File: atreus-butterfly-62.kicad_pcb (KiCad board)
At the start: 2 copper layers, 135.2 x 118.8 mm, 85 parts, among them J1 USB_OTG, J2 Conn_01x04, SW1 SW_Push, SW10 SW_Push, SW11 SW_Push, SW12 SW_Push, SW13 SW_Push, SW14 SW_Push, SW15 SW_Push, SW16 SW_Push, SW17 SW_Push, SW18 SW_Push, SW19 SW_Push, SW2 SW_Push, SW20 SW_Push, SW21 SW_Push, SW22 SW_Push, SW23 SW_Push, SW24 SW_Push, SW25 SW_Push, SW26 SW_Push, SW27 SW_Push, SW28 SW_Push, SW29 SW_Push, SW3 SW_Push, SW30 SW_Push, SW31 SW_Push, SW32 SW_Push, SW4 SW_Push, SW5 SW_Push, SW6 SW_Push, SW7 SW_Push, SW8 SW_Push, SW9 SW_Push, U1 ATMEGA32U4-MU, Y1 Crystal

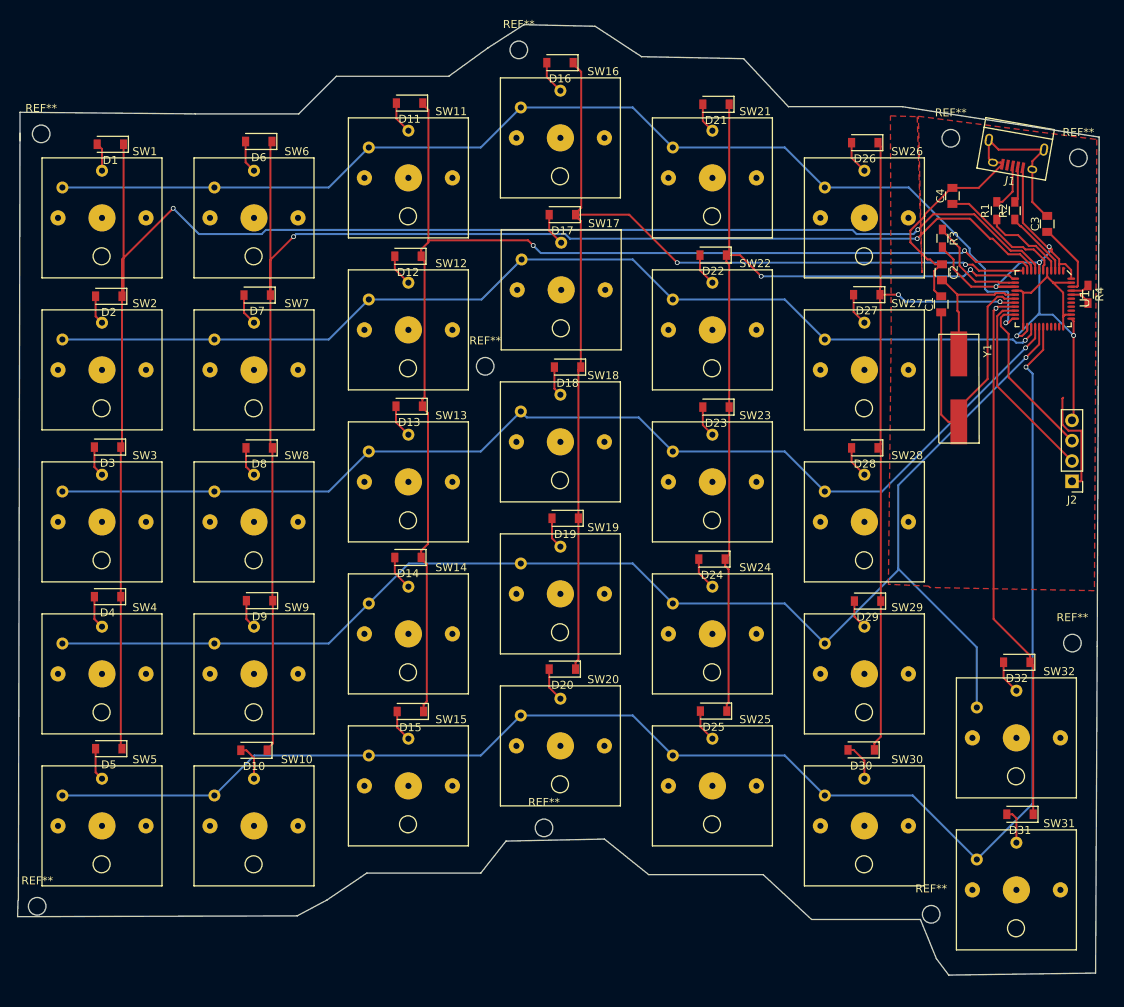
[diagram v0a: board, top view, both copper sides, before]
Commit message: delete middle keys and most traces
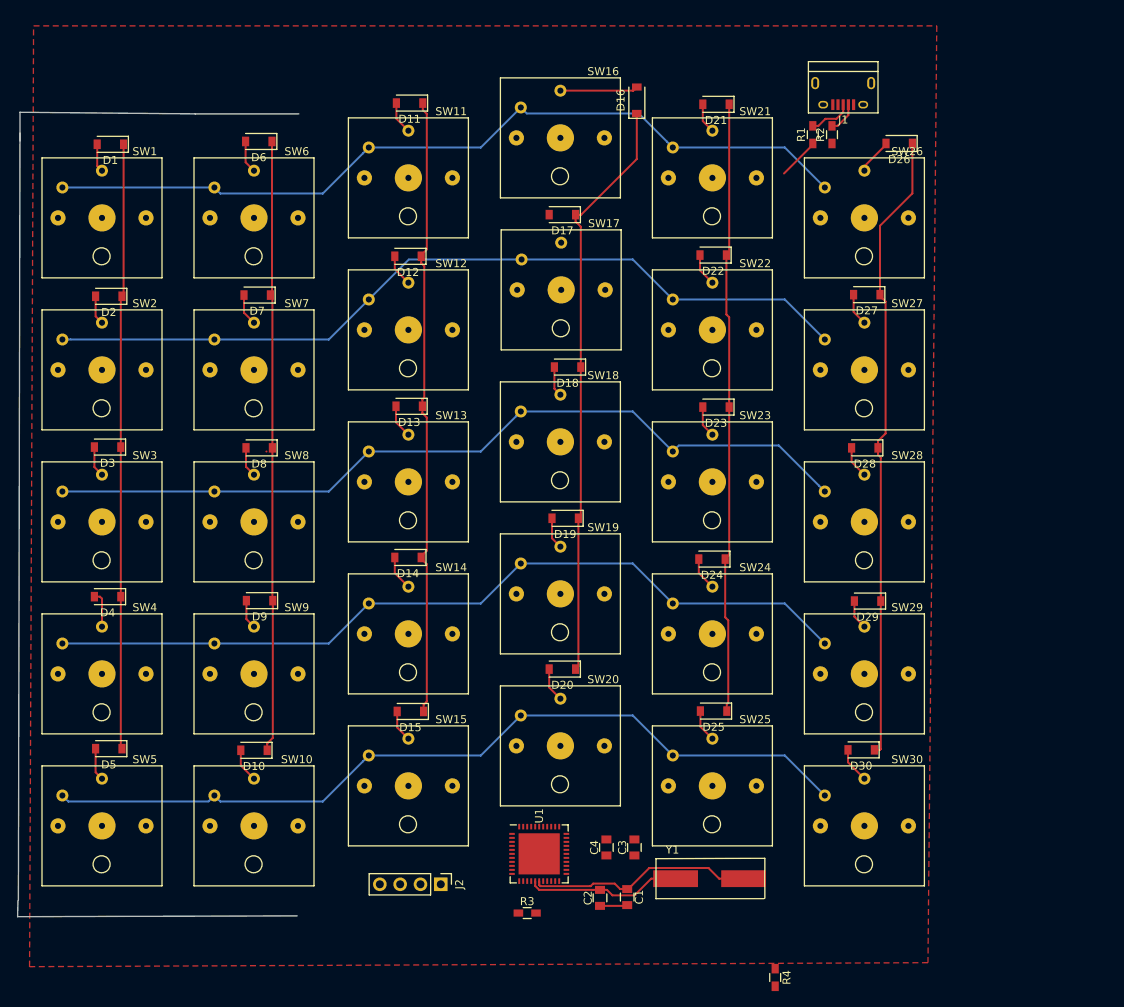
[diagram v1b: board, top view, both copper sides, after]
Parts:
- removed D31, D32: D, Diodes_SMD:D_SOD-123
- removed REF** (x9): MountingHole_2.2mm_M2, Mounting_Holes:MountingHole_2.2mm_M2
- removed SW31, SW32: SW_Push, ourglass_v7:Kailh_low_profile
- U1: footprint ourglass_v7:QFN_44 -> Housings_DFN_QFN:QFN-44-1EP_7x7mm_Pitch0.5mm
- moved R3 99.0 mm to (101.9, 152.0), turned to 0 degrees
- moved R4 93.9 mm to (132.9, 160.1)
- moved U1 93.7 mm to (103.4, 144.6), turned to 0 degrees
- moved J2 93.6 mm to (91.1, 148.4), turned to 270 degrees
- moved C3 93.5 mm to (115.3, 143.8)
- moved C4 92.2 mm to (111.8, 143.8)
- moved C2 89.1 mm to (111.0, 150.1), turned to 90 degrees
- moved C1 83.9 mm to (114.4, 150.0), turned to 270 degrees
- moved Y1 68.8 mm to (124.7, 147.7), turned to 180 degrees
- moved R1 24.9 mm to (137.6, 54.7)
- moved R2 24.7 mm to (140.0, 54.7)
- moved J1 22.8 mm to (141.4, 49.6), turned to 180 degrees
- moved D16 10.7 mm to (115.6, 50.4), turned to 90 degrees
- moved D26 4.30 mm to (148.4, 55.8)
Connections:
- U1 pad 19: /Column_7 -> Net-(U1-Pad19)
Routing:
- net /Column_1: track 203.3 -> 75.8 mm, vias 2 -> 0
- net /Column_2: track 181.8 -> 76.6 mm, vias 2 -> 0
- net /Row_5: track 196.6 -> 104.8 mm, vias 1 -> 0
- net GND: track 81.9 -> 3.44 mm
- net /Column_3: track 155.1 -> 77.8 mm, vias 2 -> 0
- net VCC: track 73.8 -> 0.00 mm, vias 5 -> 0
- net /Row_4: track 175.7 -> 103.6 mm, vias 1 -> 0
- net /Column_7: track 67.9 -> 0.00 mm, vias 1 -> 0
- net /Column_4: track 135.9 -> 73.6 mm, vias 2 -> 0
- net /Column_5: track 114.6 -> 76.6 mm, vias 2 -> 0
- net /Row_3: track 139.3 -> 104.2 mm, vias 1 -> 0
- net /Row_1: track 139.1 -> 104.2 mm, vias 1 -> 0
- net /Row_2: track 130.9 -> 103.6 mm, vias 1 -> 0
- net /Rx: track 24.5 -> 0.00 mm
- net /Tx: track 21.0 -> 0.00 mm
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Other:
- board size 135.2 x 118.8 mm -> 35.1 x 100.5 mm

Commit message: no middle keys
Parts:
- added REF**: MountingHole_2.2mm_M2, Mounting_Holes:MountingHole_2.2mm_M2, F.Cu at (41.3, 54.4)
- added REF**: MountingHole_2.2mm_M2, Mounting_Holes:MountingHole_2.2mm_M2, F.Cu at (40.6, 150.3)
- added REF**: MountingHole_2.2mm_M2, Mounting_Holes:MountingHole_2.2mm_M2, F.Cu at (151.4, 150.5)
- added REF**: MountingHole_2.2mm_M2, Mounting_Holes:MountingHole_2.2mm_M2, F.Cu at (132.7, 48.4)
- added REF**: MountingHole_2.2mm_M2, Mounting_Holes:MountingHole_2.2mm_M2, F.Cu at (93.7, 47.8)
- moved J2 111.4 mm to (151.5, 54.8), turned to 180 degrees
- moved R4 43.1 mm to (96.8, 136.5), turned to 90 degrees
- moved C4 16.1 mm to (96.0, 140.7)
- moved R3 5.86 mm to (96.6, 149.5), turned to 180 degrees
- moved C3 5.55 mm to (110.2, 141.6)
- moved D26 2.18 mm to (146.3, 55.2)
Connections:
- J1 pad 4: Net-(J1-Pad4) -> (no net)
- U1 pad 1: Net-(U1-Pad1) -> (no net)
- U1 pad 11: /Column_4 -> /Column_2
- U1 pad 12: /Column_5 -> /Column_1
- U1 pad 19: Net-(U1-Pad19) -> (no net)
- U1 pad 22: /Row_1 -> (no net)
- U1 pad 25: /Row_2 -> /Row_1
- U1 pad 26: /Row_3 -> /Row_2
- U1 pad 27: /Row_4 -> /Row_3
- U1 pad 28: /Row_5 -> /Row_4
- U1 pad 29: Net-(U1-Pad29) -> /Row_5
- U1 pad 30: Net-(U1-Pad30) -> (no net)
- U1 pad 31: Net-(U1-Pad31) -> (no net)
- U1 pad 32: Net-(U1-Pad32) -> (no net)
- U1 pad 36: Net-(U1-Pad36) -> (no net)
- U1 pad 37: Net-(U1-Pad37) -> (no net)
- U1 pad 38: Net-(U1-Pad38) -> (no net)
- U1 pad 39: Net-(U1-Pad39) -> (no net)
- U1 pad 45: (no net) -> GND
- U1 pad 8: /Column_1 -> /Column_5
- U1 pad 9: /Column_2 -> /Column_4
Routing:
- net VCC: track 0.00 -> 189.1 mm, vias 0 -> 8
- net /Tx: track 0.00 -> 141.7 mm, vias 0 -> 1
- net /Rx: track 0.00 -> 141.3 mm, vias 0 -> 1
- net /Row_1: track 104.2 -> 231.3 mm, vias 0 -> 1
- net Net-(R2-Pad1): track 0.00 -> 117.8 mm, vias 0 -> 2
- net Net-(R1-Pad1): track 5.24 -> 116.0 mm, vias 0 -> 2
- net /Row_2: track 103.6 -> 212.2 mm, vias 0 -> 2
- net /Row_3: track 104.2 -> 188.7 mm, vias 0 -> 2
- net /Row_4: track 103.6 -> 182.3 mm, vias 0 -> 3
- net /Column_1: track 75.8 -> 132.8 mm
- net /Column_6: track 79.0 -> 134.9 mm
- net /Column_5: track 76.6 -> 128.5 mm
- net /Column_4: track 73.6 -> 111.1 mm
- net /Column_2: track 76.6 -> 113.6 mm
- net /Row_5: track 104.8 -> 135.5 mm, vias 0 -> 3
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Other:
- board size 35.1 x 100.5 mm -> 115.6 x 107.3 mm
- net class Default: clearance 0.16 -> 0.15
- rule trace_clearance: 0.16 -> 0.15
